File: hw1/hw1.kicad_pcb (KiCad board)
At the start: 2 copper layers, 53.9 x 53.3 mm, 35 parts, among them J1 CONN_01X02, P1 Power, P10 CONTROL, P11 CONN_01X06, P2 Analog, P3 Digital, P4 Digital, P9 FX2LA, U1 STM32L151C6TxA, U2 MIC550x-3.3YM5, Y1 Crystal_GND24_Small

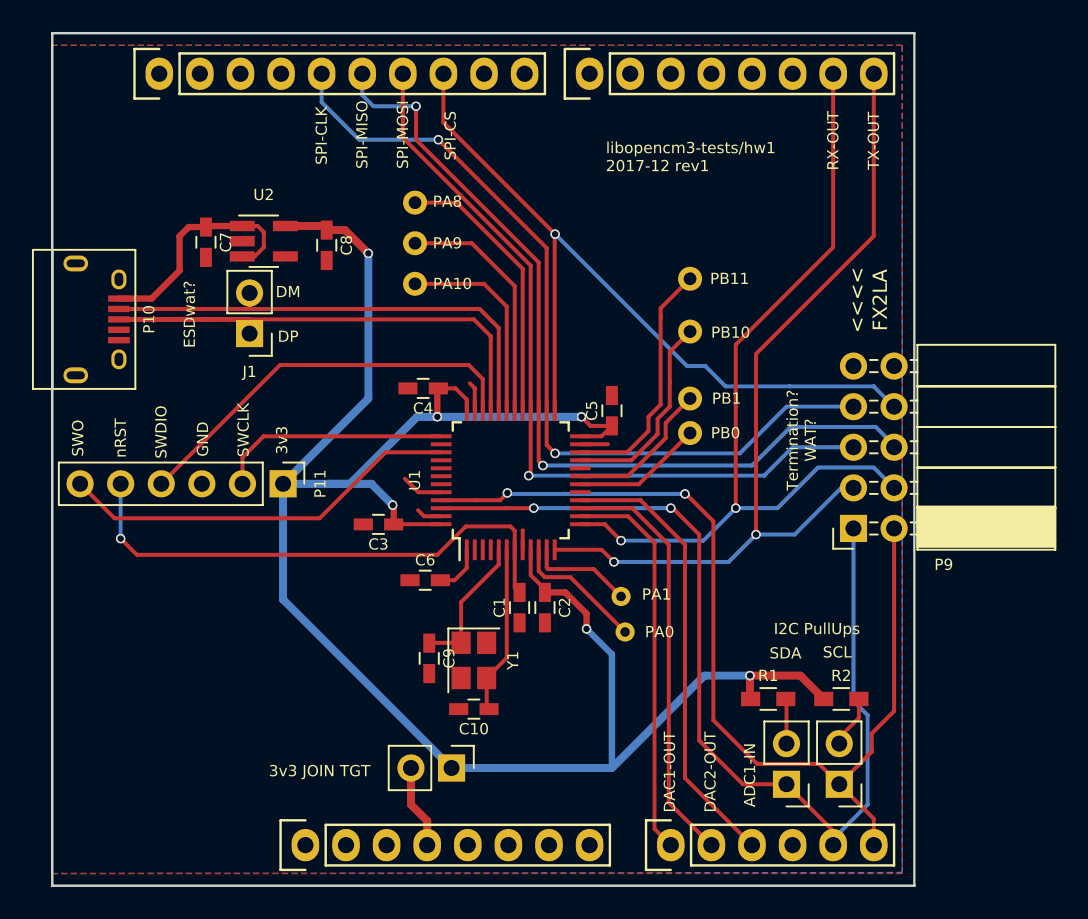
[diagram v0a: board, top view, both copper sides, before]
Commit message: hw1: use explicit 10103594-0001LF part
better fit
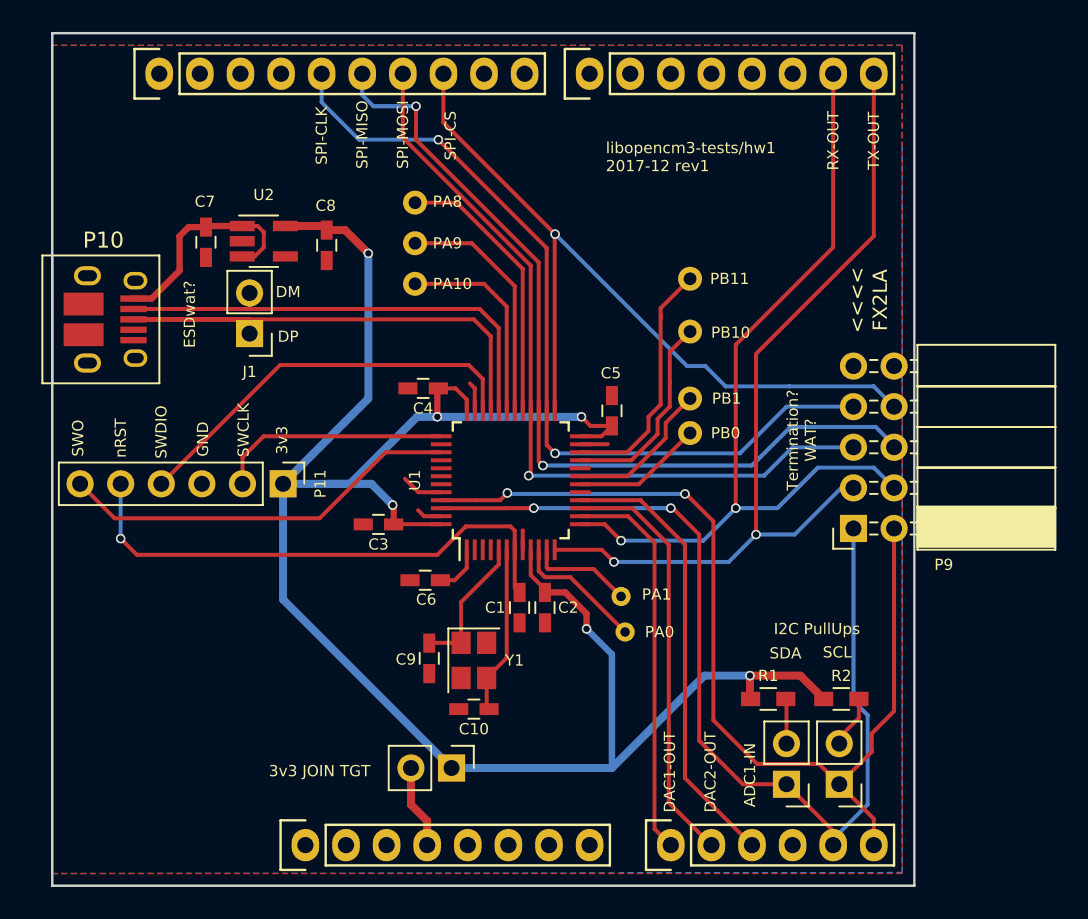
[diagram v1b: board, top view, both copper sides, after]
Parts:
- P10: footprint Connectors:USB_Micro-B -> Connectors:USB_Micro-B_10103594-0001LF
- moved P10 0.76 mm to (126.7, 90.9)
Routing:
- net /USB_DP: track 45.6 -> 43.3 mm
- net /USB_DM: track 30.0 -> 29.2 mm
- net +5V: track 14.9 -> 14.1 mm
